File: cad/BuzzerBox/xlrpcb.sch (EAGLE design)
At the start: 11 parts, among them X1 NC3, X10 NC3, X12 87758-2616, X2 NC3, X3 NC3, X4 NC3, X5 NC3, X6 NC3, X7 NC3, X8 NC3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

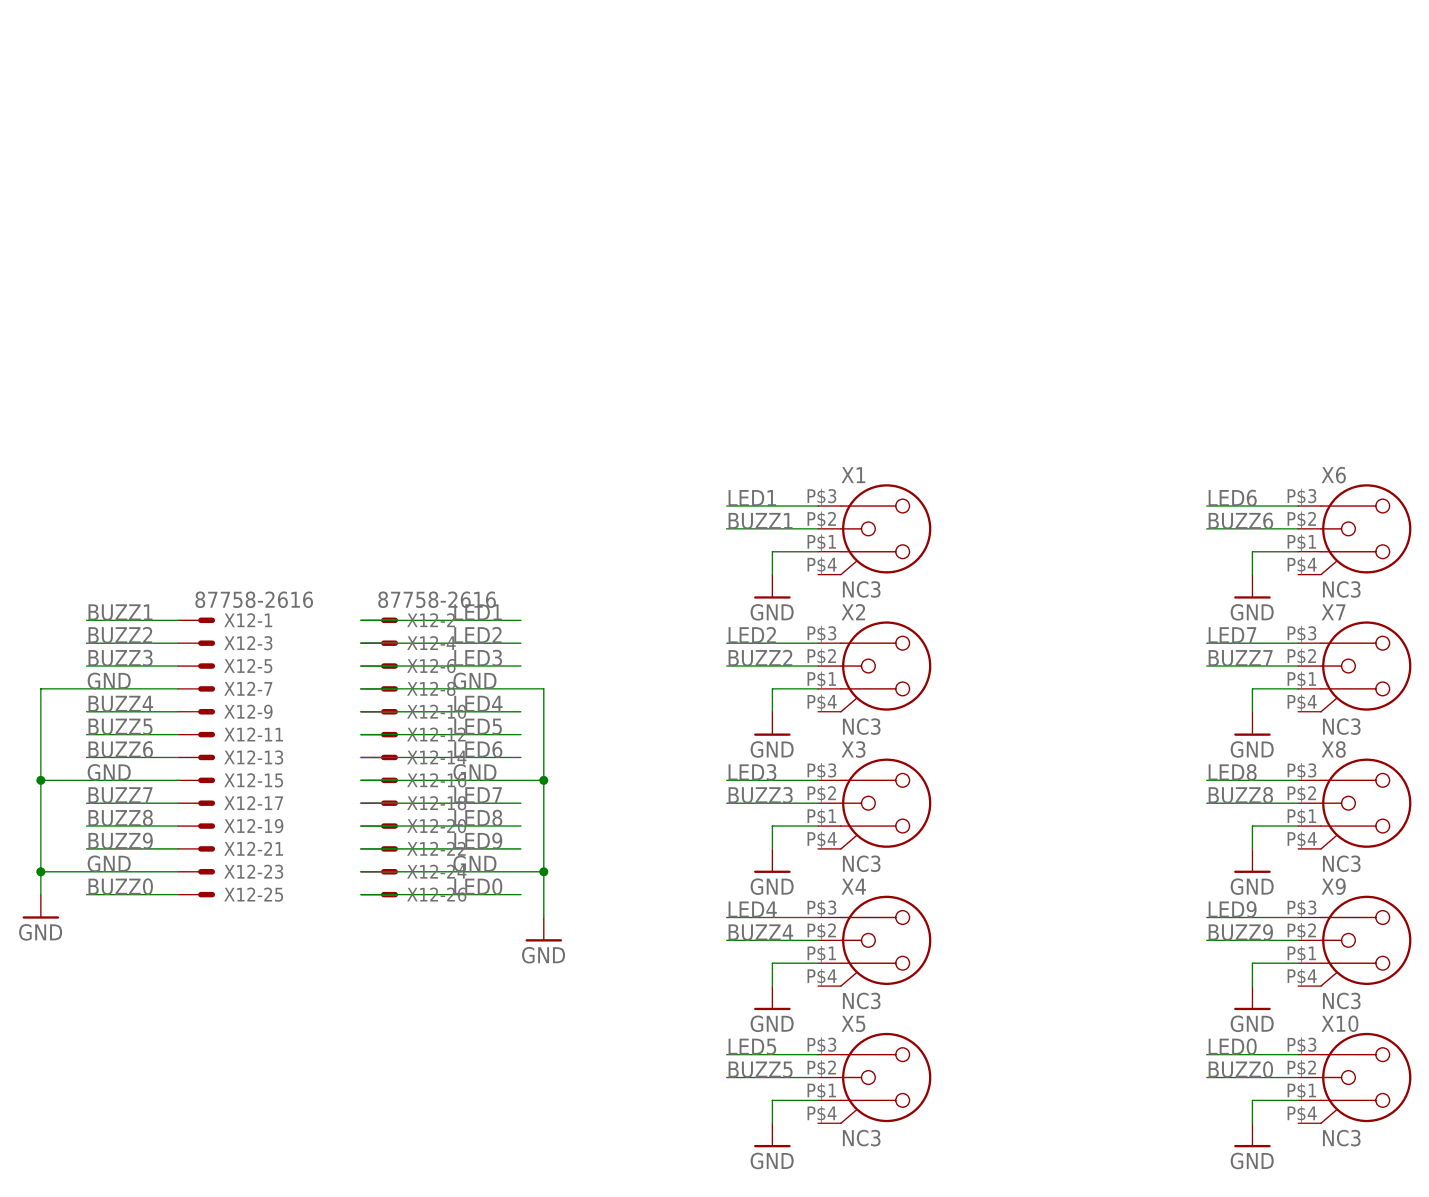
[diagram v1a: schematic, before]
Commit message: Change XLR PCB to equal spacing
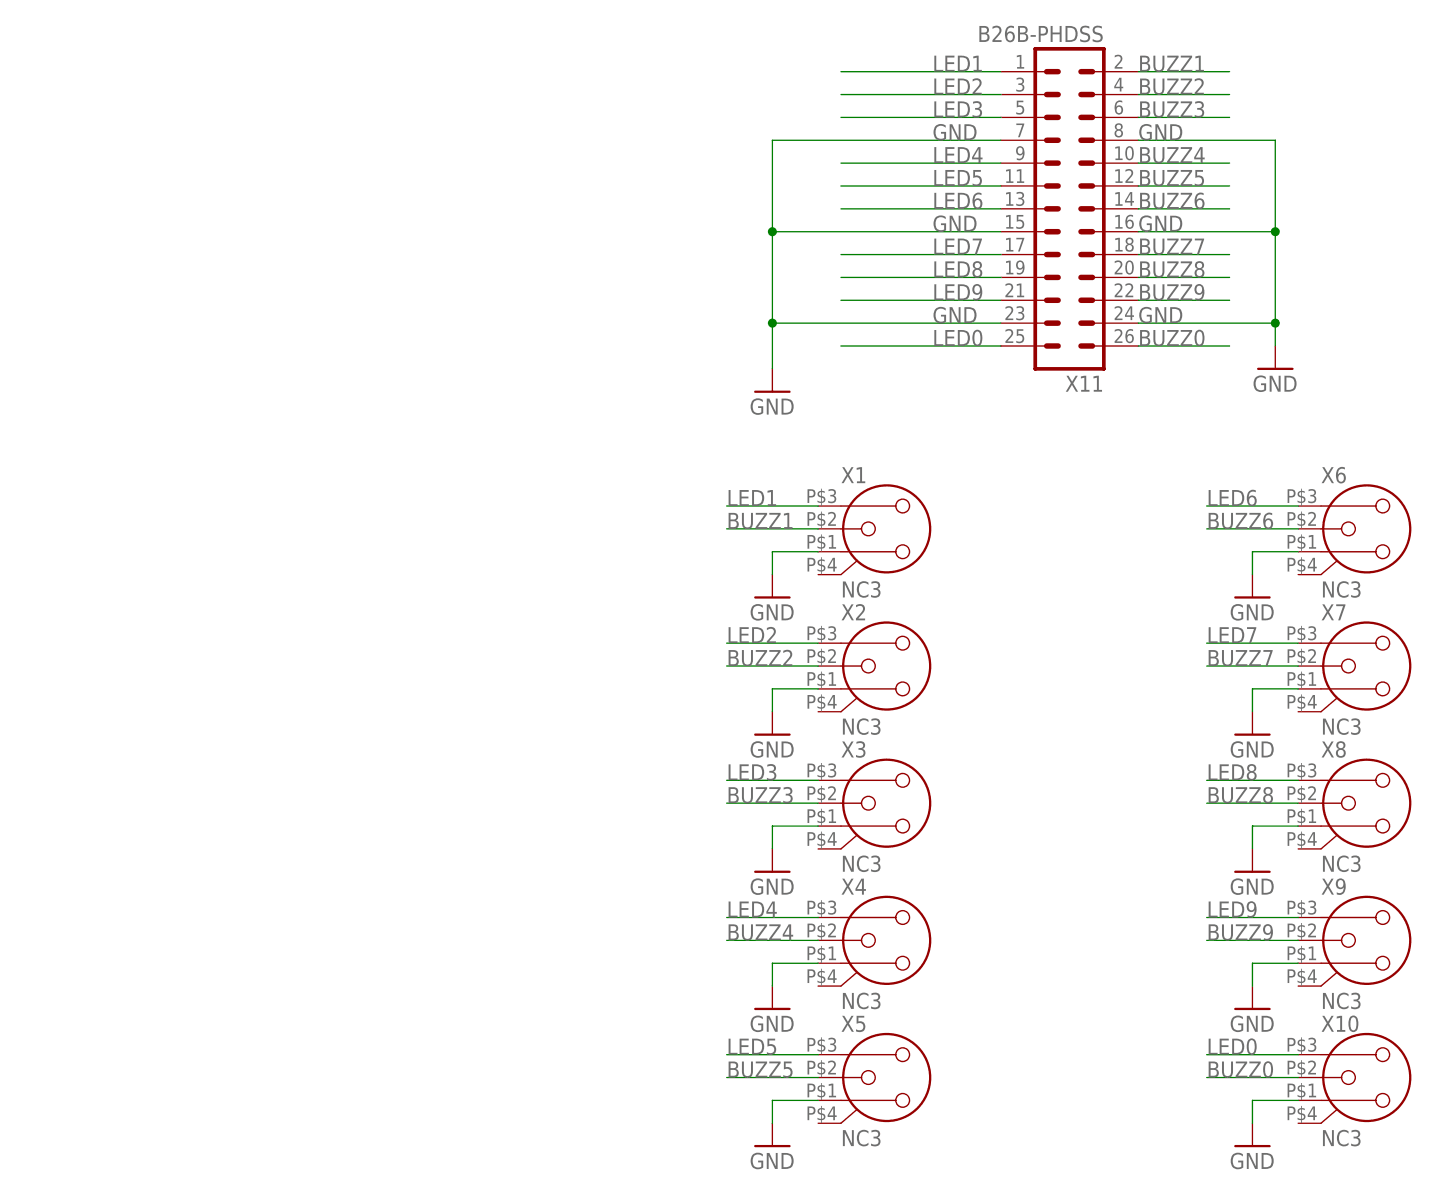
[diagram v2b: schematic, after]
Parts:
- removed X12: 87758-2616, con-molex:87758-2616
- added X11: B26B-PHDSS, con-JST PHD:B26B-PHDSS
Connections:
- net BUZZ0: now also X11.26; no longer X12-25.S
- net BUZZ1: now also X11.2; no longer X12-1.S
- net BUZZ2: now also X11.4; no longer X12-3.S
- net BUZZ3: now also X11.6; no longer X12-5.S
- net BUZZ4: now also X11.10; no longer X12-9.S
- net BUZZ5: now also X11.12; no longer X12-11.S
- net BUZZ6: now also X11.14; no longer X12-13.S
- net BUZZ7: now also X11.18; no longer X12-17.S
- net BUZZ8: now also X11.20; no longer X12-19.S
- net BUZZ9: now also X11.22; no longer X12-21.S
- net GND: now also X11.15, X11.16, X11.23, X11.24, X11.7, X11.8; no longer X12-15.S, X12-16.S, X12-23.S, X12-24.S, X12-7.S, X12-8.S
- net LED0: now also X11.25; no longer X12-26.S
- net LED1: now also X11.1; no longer X12-2.S
- net LED2: now also X11.3; no longer X12-4.S
- net LED3: now also X11.5; no longer X12-6.S
- net LED4: now also X11.9; no longer X12-10.S
- net LED5: now also X11.11; no longer X12-12.S
- net LED6: now also X11.13; no longer X12-14.S
- net LED7: now also X11.17; no longer X12-18.S
- net LED8: now also X11.19; no longer X12-20.S
- net LED9: now also X11.21; no longer X12-22.S

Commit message: Added PE to XLR Board
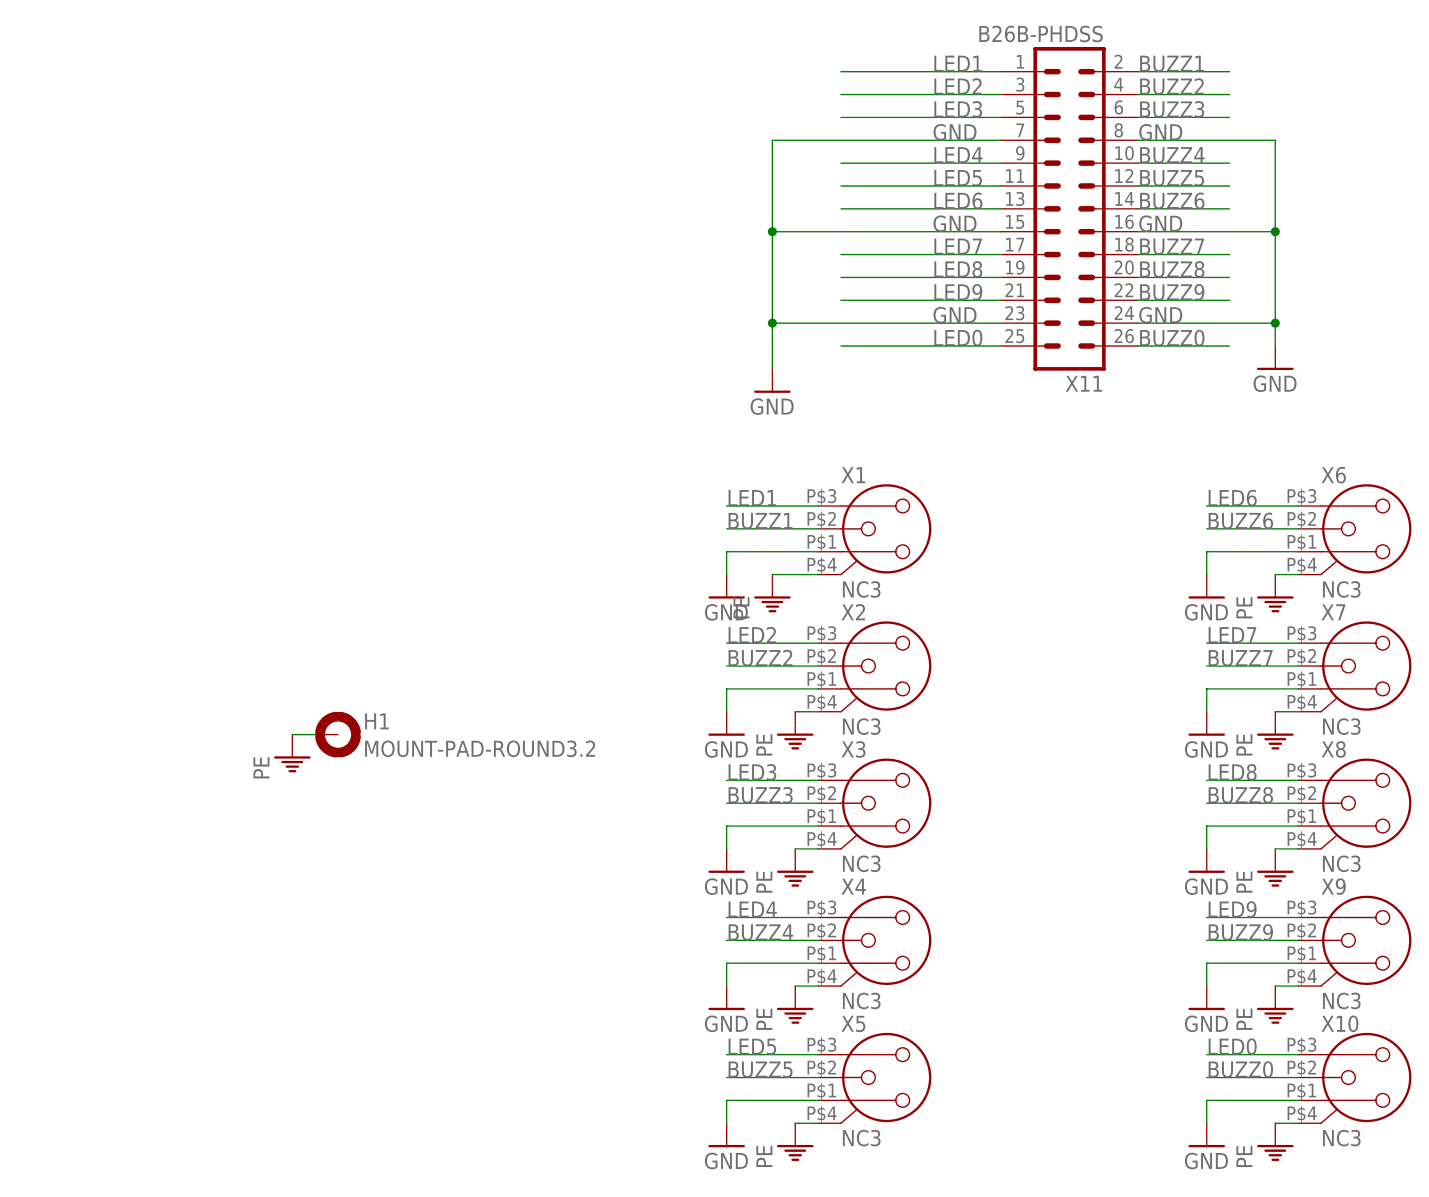
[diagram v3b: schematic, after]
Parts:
- added H1: MOUNT-PAD-ROUND3.2, holes:MOUNT-PAD-ROUND3.2
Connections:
- new net PE: H1.MOUNT, X1.G, X10.G, X2.G, X3.G, X4.G, X5.G, X6.G, X7.G, X8.G, X9.G
